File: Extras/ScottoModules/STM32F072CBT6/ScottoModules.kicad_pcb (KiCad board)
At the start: 2 copper layers, 18 parts, among them J1 USB_C, SW1 SW_Push, U1 STM32F072CBT6, U3 XC6206, U4 USBLC6-2SC6

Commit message: Update to better V2
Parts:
- removed C1, C2, C3, C4, C5: 100nF, ScottoKeebs_Components:Capacitor_0402
- removed C6: 10uF, ScottoKeebs_Components:Capacitor_0603
- added C10: 100nF, ScottoKeebs_Components:Capacitor_0402, B.Cu at (135.9, 134.6)
- added C11: 100nF, ScottoKeebs_Components:Capacitor_0402, B.Cu at (127.0, 125.7)
- added C12: 4.7uF, ScottoKeebs_Components:Capacitor_0402, B.Cu at (127.0, 124.7)
- added C13: 100nF, ScottoKeebs_Components:Capacitor_0402, B.Cu at (139.3, 131.2)
- added C14: 10nF, ScottoKeebs_Components:Capacitor_0402, B.Cu at (132.4, 134.6)
- added C15: 1uF, ScottoKeebs_Components:Capacitor_0402, B.Cu at (131.4, 134.6)
- added C16: 100nF, ScottoKeebs_Components:Capacitor_0402, B.Cu at (137.9, 124.8)
- added C17: 4.7uF, ScottoKeebs_Components:Capacitor_0402, B.Cu at (137.9, 123.8)
- added REF**: MX_1.00u_PG151101S11, ScottoKeebs_Scotto:MX_Hotswap_1.00u, B.Cu at (125.3, 101.1)
- added REF**: MX_1.00u_PG151101S11, ScottoKeebs_Scotto:MX_Hotswap_1.00u, B.Cu at (125.3, 120.1)
- added REF**: MX_1.00u_PG151101S11, ScottoKeebs_Scotto:MX_Hotswap_1.00u, B.Cu at (125.3, 139.2)
- added REF**: MX_1.00u_PG151101S11, ScottoKeebs_Scotto:MX_Hotswap_1.00u, B.Cu at (144.3, 101.1)
- added REF**: MX_1.00u_PG151101S11, ScottoKeebs_Scotto:MX_Hotswap_1.00u, B.Cu at (144.3, 139.2)
- added REF**: MX_1.00u_PG151101S11, ScottoKeebs_Scotto:MX_Hotswap_1.00u, B.Cu at (144.3, 120.1)
- moved C7 53.1 mm to (133.4, 134.6)
- moved U1 53.1 mm to (133.2, 128.5)
- moved R1 9.40 mm to (123.4, 108.5), turned to 90 degrees
- moved F1 7.09 mm to (138.4, 106.1)
- moved SW1 6.01 mm to (128.1, 109.8), turned to 0 degrees
- moved U3 2.62 mm to (137.6, 109.7)
- moved C9 2.47 mm to (137.1, 112.2)
- moved C8 2.26 mm to (138.1, 107.3)
- moved U4 1.28 mm to (134.2, 104.7)
- moved R2 1.17 mm to (132.8, 97.3)
- moved R3 0.71 mm to (136.4, 97.1), turned to -90 degrees
- moved J1 0.50 mm to (134.7, 90.6)
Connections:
- net A0 renamed /A0
- net A1 renamed /A1
- net A10 renamed /A10
- net A13 renamed /A13
- net A14 renamed /A14
- net A15 renamed /A15
- net A2 renamed /A2
- net A3 renamed /A3
- net A4 renamed /A4
- net A5 renamed /A5
- net A6 renamed /A6
- net A7 renamed /A7
- net A8 renamed /A8
- net A9 renamed /A9
- net B0 renamed /B0
- net B1 renamed /B1
- net B10 renamed /B10
- net B11 renamed /B11
- net B12 renamed /B12
- net B13 renamed /B13
- net B14 renamed /B14
- net B15 renamed /B15
- net B2 renamed /B2
- net B3 renamed /B3
- net B4 renamed /B4
- net B5 renamed /B5
- net B6 renamed /B6
- net B7 renamed /B7
- net B8 renamed /B8
- net B9 renamed /B9
- net BOOT0 renamed /BOOT0
- net C13 renamed /C13
- net C14 renamed /C14
- net C15 renamed /C15
- net F0 renamed /F0
- net F1 renamed /F1
- net Net-(U1-NRST) renamed /NRST
- J1 pad A6: D+ -> /USB_D+
- J1 pad A7: D- -> /USB_D-
- J1 pad B6: D+ -> /USB_D+
- J1 pad B7: D- -> /USB_D-
- U1 pad 32: D- -> /MCU_D-
- U1 pad 33: D+ -> /MCU_D+
- U4 pad 1: D+ -> /MCU_D+
- U4 pad 3: D- -> /MCU_D-
- U4 pad 4: D- -> /USB_D-
- U4 pad 5: +5V -> VBUS
- U4 pad 6: D+ -> /USB_D+
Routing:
- net +3.3V: track 42.7 -> 72.7 mm, vias 0 -> 7
- net /BOOT0: track 8.55 -> 35.0 mm, vias 0 -> 2
- net D-: track 23.7 -> 0.00 mm, vias 2 -> 0
- net D+: track 23.6 -> 0.00 mm
- net /MCU_D-: track 0.00 -> 18.7 mm
- net /MCU_D+: track 0.00 -> 18.6 mm
- net /USB_D-: track 0.00 -> 12.2 mm
- net /USB_D+: track 0.00 -> 12.0 mm
- net VBUS: track 13.2 -> 23.5 mm
- net +5V: track 12.9 -> 2.83 mm, vias 3 -> 0
- net GND: track 23.8 -> 18.8 mm, vias 16 -> 19
- net Net-(J1-CC1): track 1.93 -> 2.60 mm
- added copper zone on B.Cu, net GND
- added copper zone on F.Cu, net GND
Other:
- board outline added: 38.1 x 57.2 mm

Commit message: Should be final
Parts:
- moved C16 24.3 mm to (153.8, 106.4), turned to 90 degrees
- moved C17 24.3 mm to (154.8, 106.4), turned to 90 degrees
- moved C12 24.3 mm to (144.0, 107.4)
- moved C9 24.3 mm to (154.1, 94.9)
- moved F1 24.3 mm to (155.4, 88.7)
- moved J1 24.3 mm to (151.7, 73.3)
- moved R2 24.3 mm to (149.8, 80.0)
- moved REF** 24.3 mm to (142.3, 83.8)
- moved REF** 24.3 mm to (142.3, 102.8)
- moved REF** 24.3 mm to (142.3, 121.9)
- moved SW1 24.3 mm to (145.1, 92.5)
- moved U4 24.3 mm to (151.2, 87.4)
- moved C10 24.3 mm to (152.9, 117.3)
- moved C11 24.3 mm to (144.0, 108.4)
- moved C13 24.3 mm to (156.3, 113.9)
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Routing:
- net GND: track 18.8 -> 21.1 mm, vias 19 -> 20
- net +3.3V: track 72.7 -> 71.6 mm
- added copper zone on In1.Cu, net GND
- added copper zone on In2.Cu, net GND
- removed copper zone on B.Cu, net GND
- removed copper zone on F.Cu, net GND
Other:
- copper layers 2 -> 4

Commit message: Cleanup tracks and vias
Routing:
- net GND: track 21.1 -> 20.1 mm

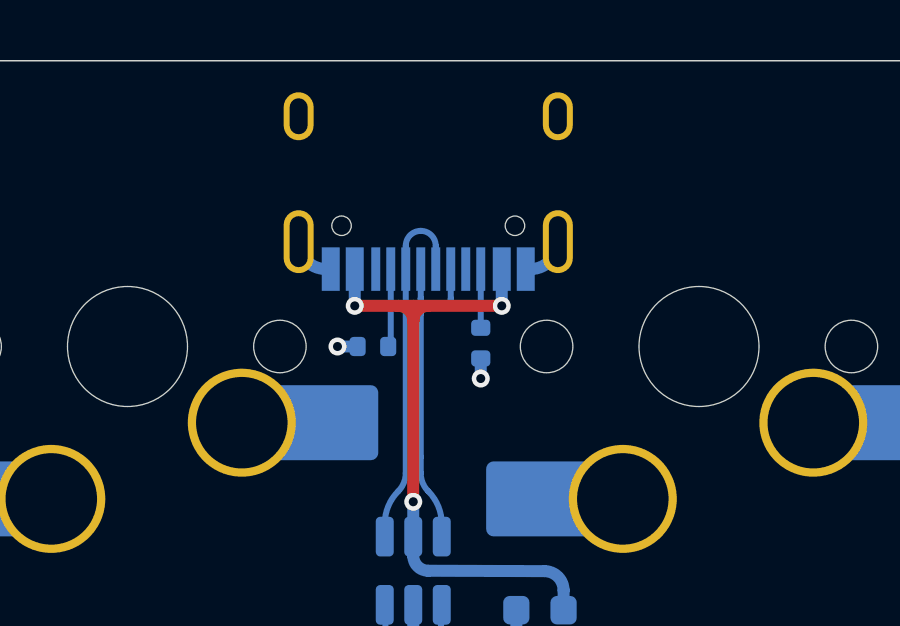
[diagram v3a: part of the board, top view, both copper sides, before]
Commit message: Convert T-Junctions to filled zones
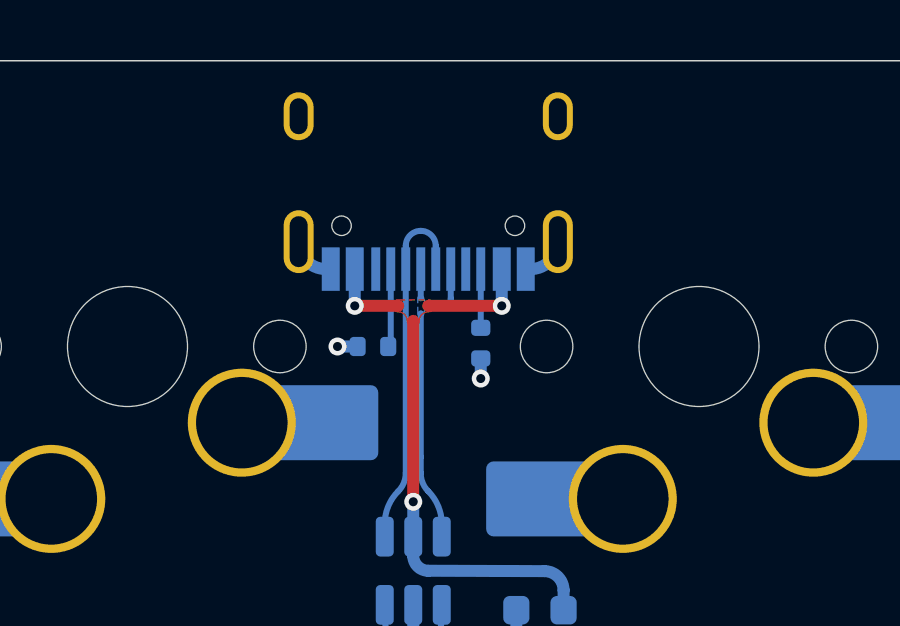
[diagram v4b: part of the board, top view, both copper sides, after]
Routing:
- net VBUS: track 23.5 -> 20.5 mm
- net /USB_D+: track 12.0 -> 10.5 mm
- added copper zone on B.Cu, net /USB_D+
- added copper zone on F.Cu, net VBUS

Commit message: Regroup
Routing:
- net /BOOT0: track 34.8 -> 22.6 mm
- net /MCU_D+: track 18.6 -> 7.85 mm
- net /MCU_D-: track 18.6 -> 7.85 mm
- net +3.3V: track 71.5 -> 62.0 mm
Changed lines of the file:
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@@
 		(pad_to_mask_clearance 0)
 		(allow_soldermask_bridges_in_footprints no)
-		(grid_origin 134.162446 125.835029)
+		(grid_origin 151.162446 96.235029)
 		(pcbplotparams
 			(layerselection 0x00010fc_ffffffff)
@@
 	)
 	(segment
-		(start 153.646196 105.030753)
-		(end 153.646196 95.589502)
-		(width 0.3)
-		(layer "F.Cu")
-		(net 2)
-	)
-	(segment
 		(start 154.56495 105.949507)
 		(end 155.804945 105.949507)
@@
 	(segment
 		(start 150.912447 90.680563)
-		(end 150.912447 106.989503)
+		(end 150.912447 96.235029)
 		(width 0.2)
 		(layer "B.Cu")
@@
 	)
 	(segment
-		(start 152.112445 88.990609)
-		(end 152.112445 88.564505)
+		(start 151.412447 90.680553)
+		(end 151.412447 96.235029)
 		(width 0.2)
 		(layer "B.Cu")
@@
 	)
 	(segment
-		(start 151.412445 106.989505)
-		(end 151.412447 90.680553)
+		(start 152.112445 88.564505)
+		(end 152.112445 88.990609)
 		(width 0.2)
 		(layer "B.Cu")
@@
 	)
 	(arc
-		(start 151.412447 90.680553)
-		(mid 151.477419 90.353915)
+		(start 152.112445 88.990609)
+		(mid 151.995493 89.578562)
 		(end 151.662445 90.077005)
 		(width 0.2)
@@
 	(arc
 		(start 151.662445 90.077005)
-		(mid 151.995493 89.578562)
-		(end 152.112445 88.990609)
+		(mid 151.477419 90.353915)
+		(end 151.412447 90.680553)
 		(width 0.2)
 		(layer "B.Cu")
@@
 		(net 25)
 	)
-	(segment
-		(start 149.912445 96.239502)
-		(end 149.912445 108.489505)
-		(width 0.2)
-		(layer "F.Cu")
-		(net 26)
-	)
 	(via
 		(at 149.912445 96.239502)
@@
 			"2dd899f4-a3d6-4298-b73f-a42b0ac49ad0" "32d51949-dded-41be-9dc6-7e1b4a73c70a"
 			"333feeea-650c-4528-91b0-71ff6da654c4" "3478b22a-dba3-408a-90c0-274084d03fd3"
-			"35e93572-df51-4139-8296-6ef6efc125d5" "41d85c7a-4bf9-49ce-bf01-6d02ab3ec021"
-			"4a5d3476-594d-4398-91d7-baf1a0de3f3d" "4d49a104-2055-4f48-864e-966259427139"
-			"4d7a8b19-f40b-46e4-a832-72d328026be7" "4f38479b-74c4-4062-a767-0c65a0abc435"
-			"583d2d4f-2b54-44f9-8499-4508727879c0" "5babc0b1-4930-482c-87d1-3d60b4dfc0bd"
-			"5eae8bfc-43eb-4de7-b784-94856166549b" "601f71f1-5c11-4851-9f49-d3aee9362802"
-			"608877cf-ee00-4a45-8063-b60bfcc5fb51" "6259d05e-9369-42cf-83cc-8dc0586eea49"
-			"640d663b-8495-4fdf-b43a-9ce9b6aa4b9a" "66df90c7-2249-4e0a-baba-0f2d6d1a3fc2"
-			"6cd1b7c8-66b8-454e-9abc-a823e6497c35" "76695977-4f31-4426-b260-d5d49b5f8072"
-			"7d363954-4ea2-4d59-8fe9-c24865247ab7" "82862ec1-30ee-4673-9b40-04ad9fbac45a"
+			"35e93572-df51-4139-8296-6ef6efc125d5" "3d5e26dc-e089-494f-8ca1-76572743cfa9"
+			"41d85c7a-4bf9-49ce-bf01-6d02ab3ec021" "4a5d3476-594d-4398-91d7-baf1a0de3f3d"
+			"4d49a104-2055-4f48-864e-966259427139" "4d7a8b19-f40b-46e4-a832-72d328026be7"
+			"4f38479b-74c4-4062-a767-0c65a0abc435" "583d2d4f-2b54-44f9-8499-4508727879c0"
+			"5babc0b1-4930-482c-87d1-3d60b4dfc0bd" "5e97a2c8-4b79-4aa2-ae83-dc0fd5c994ff"
+			"5e9d34d1-e20f-4ea1-8557-41ce451b03da" "5eae8bfc-43eb-4de7-b784-94856166549b"
+			"601f71f1-5c11-4851-9f49-d3aee9362802" "608877cf-ee00-4a45-8063-b60bfcc5fb51"
+			"6259d05e-9369-42cf-83cc-8dc0586eea49" "640d663b-8495-4fdf-b43a-9ce9b6aa4b9a"
+			"66df90c7-2249-4e0a-baba-0f2d6d1a3fc2" "6cd1b7c8-66b8-454e-9abc-a823e6497c35"
+			"76695977-4f31-4426-b260-d5d49b5f8072" "7d363954-4ea2-4d59-8fe9-c24865247ab7"
+			"7f4d5a6c-97d7-4c32-b2ec-7e152380c8ea" "82862ec1-30ee-4673-9b40-04ad9fbac45a"
 			"842bc5ad-7b5e-4bda-89de-d313322914cd" "85ec63f5-f109-40aa-816d-ec15020c7aa9"
 			"89224d77-0974-4e9e-b44a-274879bc8ae3" "89735e34-3117-4268-ac54-76d551f0f676"
@@
 			"97a6868d-03b4-4a8c-8117-101e2850c2c7" "9a6b3dc1-27ca-44a5-86cc-0dd3590fbe4b"
 			"9dff3471-9082-45d1-8f27-5046480a2cd2" "a479d8e3-f3e4-4a4e-a55e-b57521d6277b"
-			"a58c4005-74ac-49d3-9035-facb5b673911" "a734fca5-2d50-4d8c-a9f8-534ff3c6e407"
-			"a851de51-274b-4ac2-bdb5-5b4d2e746548" "aa44b589-6054-4150-832b-3ee080ccb458"
-			"b32009da-95a8-4360-861b-0c8e128324f6" "b7f8c9a2-f6a0-4f9e-bbc4-2d623f1683c1"
-			"bc2449b6-dacc-40e4-9b8e-1ae55edd8a91" "c1cd6fd8-4c68-4974-8fef-02af76e3113d"
-			"c1dfeb34-7573-4ca4-8d53-3b39499c4a0f" "c287e9f2-96df-4fb9-afee-e8c147ad5bba"
-			"c4c6f99b-aed6-4b61-99ab-26ebc8751d48" "c4d6189f-b4aa-4a83-9729-b6c977a8ba64"
-			"c504cda8-4be5-487c-9a7c-bbd46460cb5b" "c539d094-fea7-48d5-8a77-c55846fa8595"
-			"c7444152-fce1-46aa-b927-39e819918781" "ce39a813-ccf4-48c1-9db5-d5935dbd07a8"
-			"cf975467-e672-4afc-ae2a-b286debb3efe" "d0a5b8e8-b746-472c-a668-2ac6e71625eb"
-			"d0baa840-3766-4175-b92c-2778e3459bfd" "d13f2d3b-49a7-4c75-8e94-4020e17e0171"
-			"d1c75610-9b49-45cf-8508-9c6adf7c106f" "d53d8bcd-20f1-400d-9a01-43657f4e7775"
-			"d81eeb2e-7086-4f65-96bc-cd20391b3cf6" "dc4b8eec-0030-40bc-ac20-bdbabfffc22f"
-			"dcedcb90-296c-4b5f-a3c3-ca489db9c338" "de902f9e-3f28-423e-9601-dd0552641158"
-			"e4dba283-bea1-41c4-b4ed-4217c91f4dcc" "e5b37ea7-fa3b-4eab-85ce-1cae0937665c"
+			"a58c4005-74ac-49d3-9035-facb5b673911" "a606b923-6fa8-4a73-bd44-85779a778260"
+			"a734fca5-2d50-4d8c-a9f8-534ff3c6e407" "a851de51-274b-4ac2-bdb5-5b4d2e746548"
+			"aa44b589-6054-4150-832b-3ee080ccb458" "b32009da-95a8-4360-861b-0c8e128324f6"
+			"b7f8c9a2-f6a0-4f9e-bbc4-2d623f1683c1" "bc2449b6-dacc-40e4-9b8e-1ae55edd8a91"
+			"c1cd6fd8-4c68-4974-8fef-02af76e3113d" "c1dfeb34-7573-4ca4-8d53-3b39499c4a0f"
+			"c287e9f2-96df-4fb9-afee-e8c147ad5bba" "c4c6f99b-aed6-4b61-99ab-26ebc8751d48"
+			"c4d6189f-b4aa-4a83-9729-b6c977a8ba64" "c504cda8-4be5-487c-9a7c-bbd46460cb5b"
+			"c539d094-fea7-48d5-8a77-c55846fa8595" "c7444152-fce1-46aa-b927-39e819918781"
+			"ce39a813-ccf4-48c1-9db5-d5935dbd07a8" "cf975467-e672-4afc-ae2a-b286debb3efe"
+			"d0a5b8e8-b746-472c-a668-2ac6e71625eb" "d0baa840-3766-4175-b92c-2778e3459bfd"
+			"d13f2d3b-49a7-4c75-8e94-4020e17e0171" "d1c75610-9b49-45cf-8508-9c6adf7c106f"
+			"d53d8bcd-20f1-400d-9a01-43657f4e7775" "d81eeb2e-7086-4f65-96bc-cd20391b3cf6"
+			"db797990-8244-4f55-bbfa-4b07af4d430d" "dc4b8eec-0030-40bc-ac20-bdbabfffc22f"
+			"dcedcb90-296c-4b5f-a3c3-ca489db9c338" "ddb3ecb0-dbc6-48ec-9ab9-b5d7636d3e40"
+			"de902f9e-3f28-423e-9601-dd0552641158" "e4dba283-bea1-41c4-b4ed-4217c91f4dcc"
+			"e5b37ea7-fa3b-4eab-85ce-1cae0937665c" "e75be2af-a47e-4c4e-9700-85bf95f6ab13"
 			"e91e1691-2a5e-4400-a307-48ae92d6a0a3" "eb52fa47-8748-4b30-b470-f6a37d17ce92"
 			"f1aed3d4-2988-4e32-a71f-73b552d7cb13" "f2872fa4-75e5-4440-889e-facf719b69f3"
